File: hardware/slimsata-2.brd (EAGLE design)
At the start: 20.3 x 64.8 mm, 2 parts

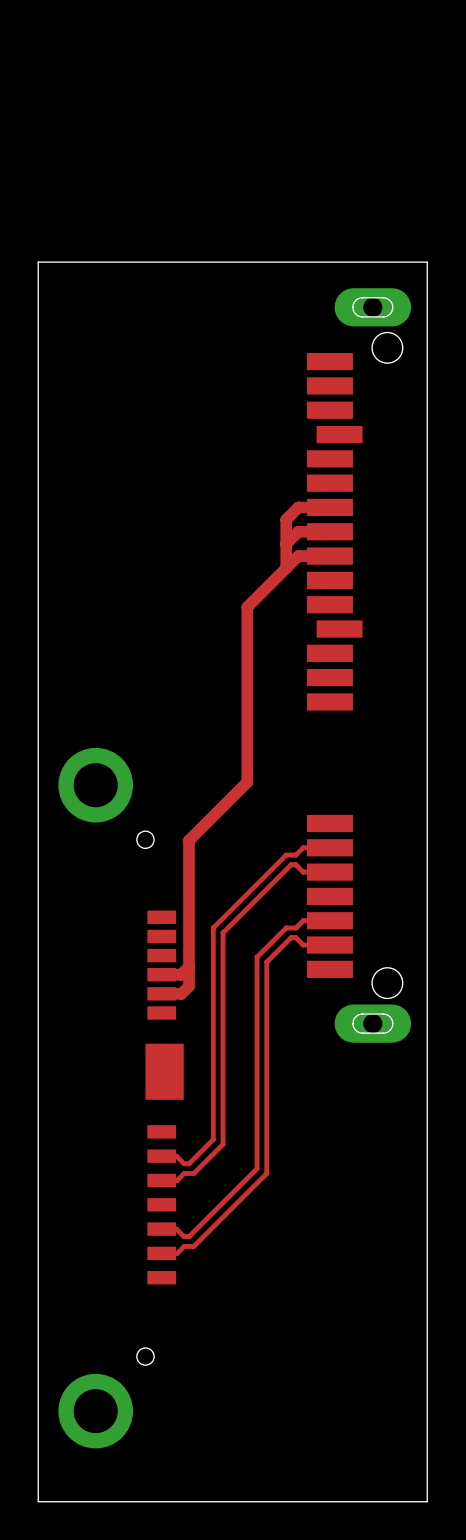
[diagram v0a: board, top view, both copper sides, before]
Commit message: Vias um Datenleitungen
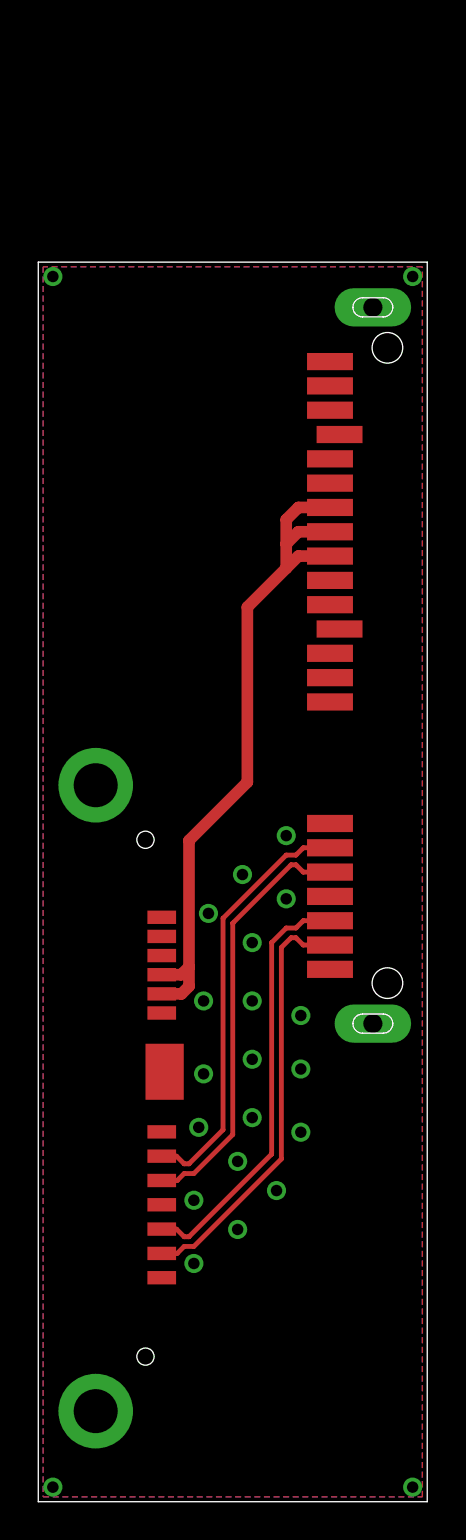
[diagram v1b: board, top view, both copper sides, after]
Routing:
- added copper zone on layer 1, net GND
- added copper zone on layer 16, net GND
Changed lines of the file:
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@@
 <wire x1="7.257" y1="12.972" x2="7.62" y2="13.335" width="0.254" layer="1"/>
 <wire x1="7.62" y1="13.335" x2="8.128" y2="13.335" width="0.254" layer="1"/>
-<wire x1="8.128" y1="13.335" x2="11.938" y2="17.145" width="0.254" layer="1"/>
-<wire x1="11.938" y1="17.145" x2="11.938" y2="28.194" width="0.254" layer="1"/>
-<wire x1="11.938" y1="28.194" x2="13.208" y2="29.464" width="0.254" layer="1"/>
+<wire x1="8.128" y1="13.335" x2="12.7" y2="17.907" width="0.254" layer="1"/>
+<wire x1="12.7" y1="17.907" x2="12.7" y2="28.956" width="0.254" layer="1"/>
+<wire x1="12.7" y1="28.956" x2="13.208" y2="29.464" width="0.254" layer="1"/>
 <wire x1="15.24" y1="29.083" x2="13.843" y2="29.083" width="0.254" layer="1"/>
 <wire x1="13.843" y1="29.083" x2="13.462" y2="29.464" width="0.254" layer="1"/>
@@
 <wire x1="7.221" y1="14.242" x2="7.62" y2="13.843" width="0.254" layer="1"/>
 <wire x1="7.62" y1="13.843" x2="7.874" y2="13.843" width="0.254" layer="1"/>
-<wire x1="7.874" y1="13.843" x2="11.43" y2="17.399" width="0.254" layer="1"/>
-<wire x1="11.43" y1="17.399" x2="11.43" y2="28.448" width="0.254" layer="1"/>
-<wire x1="11.43" y1="28.448" x2="12.954" y2="29.972" width="0.254" layer="1"/>
+<wire x1="7.874" y1="13.843" x2="12.192" y2="18.161" width="0.254" layer="1"/>
+<wire x1="12.192" y1="18.161" x2="12.192" y2="29.21" width="0.254" layer="1"/>
+<wire x1="12.192" y1="29.21" x2="12.954" y2="29.972" width="0.254" layer="1"/>
 <wire x1="15.24" y1="30.353" x2="13.843" y2="30.353" width="0.254" layer="1"/>
 <wire x1="13.843" y1="30.353" x2="13.462" y2="29.972" width="0.254" layer="1"/>
@@
 <wire x1="7.257" y1="16.782" x2="7.62" y2="17.145" width="0.254" layer="1"/>
 <wire x1="7.62" y1="17.145" x2="8.128" y2="17.145" width="0.254" layer="1"/>
-<wire x1="8.128" y1="17.145" x2="9.652" y2="18.669" width="0.254" layer="1"/>
-<wire x1="9.652" y1="29.718" x2="9.652" y2="18.669" width="0.254" layer="1"/>
-<wire x1="9.652" y1="29.718" x2="13.208" y2="33.274" width="0.254" layer="1"/>
+<wire x1="8.128" y1="17.145" x2="10.16" y2="19.177" width="0.254" layer="1"/>
+<wire x1="10.16" y1="30.226" x2="10.16" y2="19.177" width="0.254" layer="1"/>
+<wire x1="10.16" y1="30.226" x2="13.208" y2="33.274" width="0.254" layer="1"/>
 <wire x1="13.462" y1="33.274" x2="13.208" y2="33.274" width="0.254" layer="1"/>
 <wire x1="15.24" y1="32.893" x2="13.843" y2="32.893" width="0.254" layer="1"/>
@@
 <wire x1="7.221" y1="18.052" x2="7.62" y2="17.653" width="0.254" layer="1"/>
 <wire x1="7.62" y1="17.653" x2="7.874" y2="17.653" width="0.254" layer="1"/>
-<wire x1="7.874" y1="17.653" x2="9.144" y2="18.923" width="0.254" layer="1"/>
-<wire x1="9.144" y1="29.972" x2="9.144" y2="18.923" width="0.254" layer="1"/>
-<wire x1="9.144" y1="29.972" x2="12.954" y2="33.782" width="0.254" layer="1"/>
+<wire x1="7.874" y1="17.653" x2="9.652" y2="19.431" width="0.254" layer="1"/>
+<wire x1="9.652" y1="30.48" x2="9.652" y2="19.431" width="0.254" layer="1"/>
+<wire x1="9.652" y1="30.48" x2="12.954" y2="33.782" width="0.254" layer="1"/>
 <wire x1="15.24" y1="34.163" x2="13.843" y2="34.163" width="0.254" layer="1"/>
 <wire x1="13.843" y1="34.163" x2="13.462" y2="33.782" width="0.254" layer="1"/>
@@
 <contactref element="CON2" pad="P6"/>
 <contactref element="CON2" pad="P5"/>
-<wire x1="15.74" y1="55.753" x2="17.48" y2="62.398" width="0" layer="19" extent="1-1"/>
-<wire x1="15.24" y1="53.213" x2="15.74" y2="55.753" width="0" layer="19" extent="1-1"/>
-<wire x1="15.24" y1="48.133" x2="15.24" y2="53.213" width="0" layer="19" extent="1-1"/>
-<wire x1="15.24" y1="46.863" x2="15.24" y2="48.133" width="0" layer="19" extent="1-1"/>
-<wire x1="15.74" y1="45.593" x2="15.24" y2="46.863" width="0" layer="19" extent="1-1"/>
-<wire x1="15.24" y1="35.433" x2="15.74" y2="45.593" width="0" layer="19" extent="1-1"/>
-<wire x1="15.24" y1="31.623" x2="15.24" y2="35.433" width="0" layer="19" extent="1-1"/>
-<wire x1="15.24" y1="27.813" x2="15.24" y2="31.623" width="0" layer="19" extent="1-1"/>
-<wire x1="17.48" y1="24.978" x2="15.24" y2="27.813" width="0" layer="19" extent="1-1"/>
-<wire x1="3" y1="37.432" x2="15.24" y2="27.813" width="0" layer="19" extent="1-1"/>
-<wire x1="6.45" y1="30.532" x2="3" y2="37.432" width="0" layer="19" extent="1-1"/>
-<wire x1="6.45" y1="29.532" x2="6.45" y2="30.532" width="0" layer="19" extent="1-1"/>
-<wire x1="6.6" y1="22.462" x2="6.45" y2="29.532" width="0" layer="19" extent="1-1"/>
-<wire x1="6.45" y1="19.322" x2="6.6" y2="22.462" width="0" layer="19" extent="1-1"/>
-<wire x1="6.45" y1="15.512" x2="6.45" y2="19.322" width="0" layer="19" extent="1-1"/>
-<wire x1="6.45" y1="11.702" x2="6.45" y2="15.512" width="0" layer="19" extent="1-1"/>
-<wire x1="3" y1="4.732" x2="6.45" y2="11.702" width="0" layer="19" extent="1-1"/>
+<polygon width="0.6096" layer="1">
+<vertex x="0.254" y="0.254"/>
+<vertex x="20.066" y="0.254"/>
+<vertex x="20.066" y="64.516"/>
+<vertex x="0.254" y="64.516"/>
+</polygon>
+<polygon width="0.6096" layer="16">
+<vertex x="0.254" y="0.254"/>
+<vertex x="20.066" y="0.254"/>
+<vertex x="20.066" y="64.516"/>
+<vertex x="0.254" y="64.516"/>
+</polygon>
+<via x="0.762" y="0.762" extent="1-16" drill="0.6"/>
+<via x="19.558" y="0.762" extent="1-16" drill="0.6"/>
+<via x="0.762" y="64.008" extent="1-16" drill="0.6"/>
+<via x="19.558" y="64.008" extent="1-16" drill="0.6"/>
+<via x="8.128" y="15.748" extent="1-16" drill="0.6"/>
+<via x="10.414" y="17.78" extent="1-16" drill="0.6"/>
+<via x="11.176" y="20.066" extent="1-16" drill="0.6"/>
+<via x="11.176" y="23.114" extent="1-16" drill="0.6"/>
+<via x="11.176" y="26.162" extent="1-16" drill="0.6"/>
+<via x="11.176" y="29.21" extent="1-16" drill="0.6"/>
+<via x="12.954" y="31.496" extent="1-16" drill="0.6"/>
+<via x="8.382" y="19.558" extent="1-16" drill="0.6"/>
+<via x="8.636" y="22.352" extent="1-16" drill="0.6"/>
+<via x="8.636" y="26.162" extent="1-16" drill="0.6"/>
+<via x="8.89" y="30.734" extent="1-16" drill="0.6"/>
+<via x="10.668" y="32.766" extent="1-16" drill="0.6"/>
+<via x="12.954" y="34.798" extent="1-16" drill="0.6"/>
+<via x="8.128" y="12.446" extent="1-16" drill="0.6"/>
+<via x="10.414" y="14.224" extent="1-16" drill="0.6"/>
+<via x="12.446" y="16.256" extent="1-16" drill="0.6"/>
+<via x="13.716" y="19.304" extent="1-16" drill="0.6"/>
+<via x="13.716" y="22.606" extent="1-16" drill="0.6"/>
+<via x="13.716" y="25.4" extent="1-16" drill="0.6"/>
 </signal>
 </signals>

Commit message: Masse von Hand verlegt
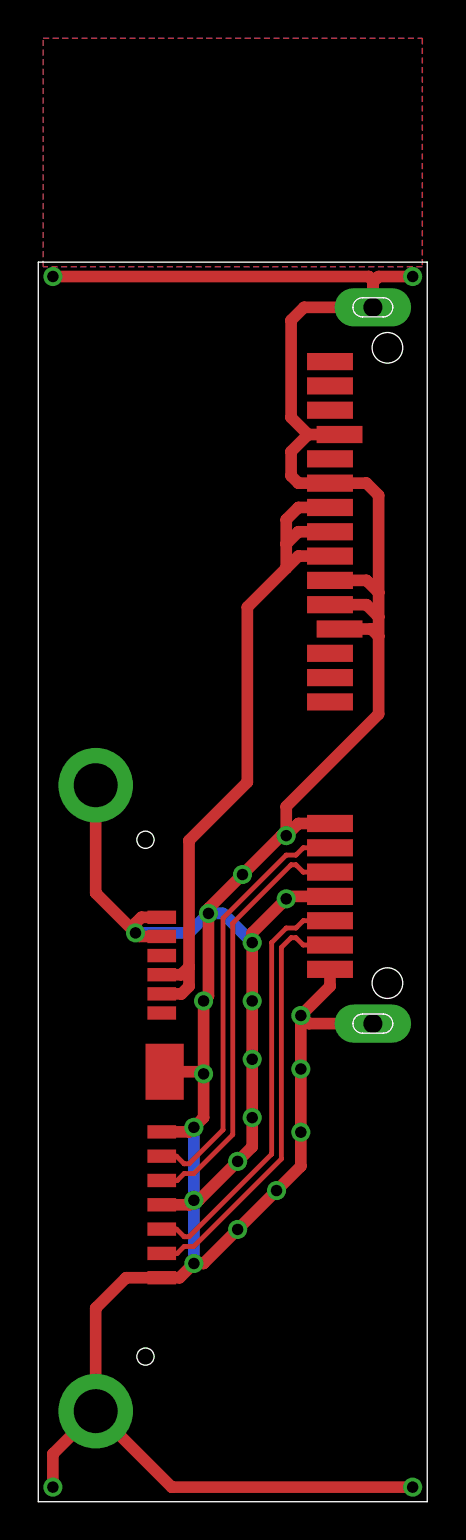
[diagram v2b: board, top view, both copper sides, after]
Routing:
- net GND: track 0.00 -> 198.4 mm, vias 23 -> 24
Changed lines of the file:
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@@
 <contactref element="CON2" pad="P5"/>
 <polygon width="0.6096" layer="1">
-<vertex x="0.254" y="0.254"/>
-<vertex x="20.066" y="0.254"/>
+<vertex x="0.254" y="76.454"/>
+<vertex x="20.066" y="76.454"/>
 <vertex x="20.066" y="64.516"/>
 <vertex x="0.254" y="64.516"/>
 </polygon>
 <polygon width="0.6096" layer="16">
-<vertex x="0.254" y="0.254"/>
-<vertex x="20.066" y="0.254"/>
+<vertex x="0.254" y="76.454"/>
+<vertex x="20.066" y="76.454"/>
 <vertex x="20.066" y="64.516"/>
 <vertex x="0.254" y="64.516"/>
@@
 <via x="11.176" y="29.21" extent="1-16" drill="0.6"/>
 <via x="12.954" y="31.496" extent="1-16" drill="0.6"/>
-<via x="8.382" y="19.558" extent="1-16" drill="0.6"/>
+<via x="8.128" y="19.558" extent="1-16" drill="0.6"/>
 <via x="8.636" y="22.352" extent="1-16" drill="0.6"/>
 <via x="8.636" y="26.162" extent="1-16" drill="0.6"/>
@@
 <via x="13.716" y="22.606" extent="1-16" drill="0.6"/>
 <via x="13.716" y="25.4" extent="1-16" drill="0.6"/>
+<wire x1="6.45" y1="11.702" x2="7.384" y2="11.702" width="0.6096" layer="1"/>
+<wire x1="8.128" y1="12.446" x2="8.636" y2="12.446" width="0.6096" layer="1"/>
+<wire x1="8.636" y1="12.446" x2="10.414" y2="14.224" width="0.6096" layer="1"/>
+<wire x1="10.414" y1="14.224" x2="12.446" y2="16.256" width="0.6096" layer="1"/>
+<wire x1="12.446" y1="16.256" x2="13.716" y2="17.526" width="0.6096" layer="1"/>
+<wire x1="13.716" y1="17.526" x2="13.716" y2="19.304" width="0.6096" layer="1"/>
+<wire x1="13.716" y1="22.606" x2="13.716" y2="19.304" width="0.6096" layer="1"/>
+<wire x1="13.716" y1="25.4" x2="13.716" y2="22.606" width="0.6096" layer="1"/>
+<wire x1="6.45" y1="15.512" x2="7.892" y2="15.512" width="0.6096" layer="1"/>
+<wire x1="7.892" y1="15.512" x2="8.128" y2="15.748" width="0.6096" layer="1"/>
+<wire x1="8.128" y1="15.748" x2="8.382" y2="15.748" width="0.6096" layer="1"/>
+<wire x1="8.382" y1="15.748" x2="10.414" y2="17.78" width="0.6096" layer="1"/>
+<wire x1="10.414" y1="17.78" x2="11.176" y2="18.542" width="0.6096" layer="1"/>
+<wire x1="11.176" y1="18.542" x2="11.176" y2="20.066" width="0.6096" layer="1"/>
+<wire x1="11.176" y1="23.114" x2="11.176" y2="20.066" width="0.6096" layer="1"/>
+<wire x1="11.176" y1="23.114" x2="11.176" y2="26.162" width="0.6096" layer="1"/>
+<wire x1="11.176" y1="26.162" x2="11.176" y2="29.21" width="0.6096" layer="1"/>
+<wire x1="11.176" y1="29.21" x2="11.176" y2="29.718" width="0.6096" layer="1"/>
+<wire x1="11.176" y1="29.718" x2="12.954" y2="31.496" width="0.6096" layer="1"/>
+<wire x1="15.24" y1="31.623" x2="13.081" y2="31.623" width="0.6096" layer="1"/>
+<wire x1="13.081" y1="31.623" x2="12.954" y2="31.496" width="0.6096" layer="1"/>
+<wire x1="15.24" y1="27.813" x2="15.24" y2="26.924" width="0.6096" layer="1"/>
+<wire x1="15.24" y1="26.924" x2="13.716" y2="25.4" width="0.6096" layer="1"/>
+<wire x1="17.48" y1="24.978" x2="14.138" y2="24.978" width="0.6096" layer="1"/>
+<wire x1="14.138" y1="24.978" x2="13.716" y2="25.4" width="0.6096" layer="1"/>
+<wire x1="15.24" y1="35.433" x2="13.589" y2="35.433" width="0.6096" layer="1"/>
+<wire x1="13.589" y1="35.433" x2="12.954" y2="34.798" width="0.6096" layer="1"/>
+<wire x1="12.954" y1="34.798" x2="12.7" y2="34.798" width="0.6096" layer="1"/>
+<wire x1="12.7" y1="34.798" x2="10.668" y2="32.766" width="0.6096" layer="1"/>
+<wire x1="8.89" y1="30.734" x2="8.89" y2="30.988" width="0.6096" layer="1"/>
+<wire x1="8.89" y1="30.988" x2="10.668" y2="32.766" width="0.6096" layer="1"/>
+<wire x1="8.89" y1="26.416" x2="8.636" y2="26.162" width="0.6096" layer="1"/>
+<wire x1="8.636" y1="22.352" x2="8.636" y2="26.162" width="0.6096" layer="1"/>
+<wire x1="6.45" y1="29.532" x2="5.266" y2="29.532" width="0.6096" layer="1"/>
+<wire x1="5.266" y1="29.532" x2="5.08" y2="29.718" width="0.6096" layer="1"/>
+<wire x1="6.45" y1="30.532" x2="5.386" y2="30.532" width="0.6096" layer="1"/>
+<wire x1="5.386" y1="30.532" x2="5.08" y2="30.226" width="0.6096" layer="1"/>
+<via x="5.08" y="29.718" extent="1-16" drill="0.6"/>
+<wire x1="5.08" y1="29.718" x2="7.874" y2="29.718" width="0.6096" layer="16"/>
+<wire x1="7.874" y1="29.718" x2="8.89" y2="30.734" width="0.6096" layer="16"/>
+<wire x1="5.08" y1="30.226" x2="5.08" y2="29.718" width="0.6096" layer="1"/>
+<wire x1="3" y1="37.432" x2="3" y2="31.798" width="0.6096" layer="1"/>
+<wire x1="3" y1="31.798" x2="5.08" y2="29.718" width="0.6096" layer="1"/>
+<wire x1="3" y1="4.732" x2="3" y2="10.112" width="0.6096" layer="1"/>
+<wire x1="3" y1="10.112" x2="4.59" y2="11.702" width="0.6096" layer="1"/>
+<wire x1="6.45" y1="11.702" x2="4.59" y2="11.702" width="0.6096" layer="1"/>
+<wire x1="0.762" y1="0.762" x2="0.762" y2="2.494" width="0.6096" layer="1"/>
+<wire x1="0.762" y1="2.494" x2="3" y2="4.732" width="0.6096" layer="1"/>
+<wire x1="19.558" y1="0.762" x2="6.97" y2="0.762" width="0.6096" layer="1"/>
+<wire x1="6.97" y1="0.762" x2="3" y2="4.732" width="0.6096" layer="1"/>
+<wire x1="17.48" y1="62.398" x2="17.48" y2="63.708" width="0.6096" layer="1"/>
+<wire x1="17.48" y1="63.708" x2="17.78" y2="64.008" width="0.6096" layer="1"/>
+<wire x1="17.78" y1="64.008" x2="19.558" y2="64.008" width="0.6096" layer="1"/>
+<wire x1="17.48" y1="62.398" x2="17.48" y2="63.8" width="0.6096" layer="1"/>
+<wire x1="17.48" y1="63.8" x2="17.272" y2="64.008" width="0.6096" layer="1"/>
+<wire x1="17.272" y1="64.008" x2="0.762" y2="64.008" width="0.6096" layer="1"/>
+<wire x1="17.48" y1="62.398" x2="13.884" y2="62.398" width="0.6096" layer="1"/>
+<wire x1="13.884" y1="62.398" x2="13.208" y2="61.722" width="0.6096" layer="1"/>
+<wire x1="13.208" y1="61.722" x2="13.208" y2="56.642" width="0.6096" layer="1"/>
+<wire x1="14.097" y1="55.753" x2="13.208" y2="56.642" width="0.6096" layer="1"/>
+<wire x1="15.74" y1="55.753" x2="14.097" y2="55.753" width="0.6096" layer="1"/>
+<wire x1="14.097" y1="55.753" x2="13.208" y2="54.864" width="0.6096" layer="1"/>
+<wire x1="13.208" y1="54.864" x2="13.208" y2="53.594" width="0.6096" layer="1"/>
+<wire x1="15.24" y1="53.213" x2="13.589" y2="53.213" width="0.6096" layer="1"/>
+<wire x1="13.589" y1="53.213" x2="13.208" y2="53.594" width="0.6096" layer="1"/>
+<wire x1="15.24" y1="53.213" x2="17.145" y2="53.213" width="0.6096" layer="1"/>
+<wire x1="17.145" y1="53.213" x2="17.78" y2="52.578" width="0.6096" layer="1"/>
+<wire x1="17.78" y1="52.578" x2="17.78" y2="47.498" width="0.6096" layer="1"/>
+<wire x1="17.78" y1="47.498" x2="17.78" y2="46.228" width="0.6096" layer="1"/>
+<wire x1="17.78" y1="46.228" x2="17.78" y2="45.212" width="0.6096" layer="1"/>
+<wire x1="17.78" y1="45.212" x2="17.78" y2="41.148" width="0.6096" layer="1"/>
+<wire x1="15.24" y1="48.133" x2="17.145" y2="48.133" width="0.6096" layer="1"/>
+<wire x1="17.145" y1="48.133" x2="17.78" y2="47.498" width="0.6096" layer="1"/>
+<wire x1="15.24" y1="46.863" x2="17.145" y2="46.863" width="0.6096" layer="1"/>
+<wire x1="17.145" y1="46.863" x2="17.78" y2="46.228" width="0.6096" layer="1"/>
+<wire x1="15.74" y1="45.593" x2="17.399" y2="45.593" width="0.6096" layer="1"/>
+<wire x1="17.399" y1="45.593" x2="17.78" y2="45.212" width="0.6096" layer="1"/>
+<wire x1="17.78" y1="41.148" x2="12.954" y2="36.322" width="0.6096" layer="1"/>
+<wire x1="12.954" y1="36.322" x2="12.954" y2="34.798" width="0.6096" layer="1"/>
+<wire x1="6.45" y1="19.322" x2="7.892" y2="19.322" width="0.6096" layer="1"/>
+<wire x1="7.892" y1="19.322" x2="8.128" y2="19.558" width="0.6096" layer="1"/>
+<wire x1="8.89" y1="30.734" x2="9.652" y2="30.734" width="0.6096" layer="16"/>
+<wire x1="9.652" y1="30.734" x2="11.176" y2="29.21" width="0.6096" layer="16"/>
+<wire x1="8.89" y1="26.416" x2="8.89" y2="30.734" width="0.6096" layer="1"/>
+<wire x1="8.128" y1="19.558" x2="8.128" y2="15.748" width="0.6096" layer="16"/>
+<wire x1="8.128" y1="12.446" x2="8.128" y2="15.748" width="0.6096" layer="16"/>
+<wire x1="7.384" y1="11.702" x2="8.128" y2="12.446" width="0.6096" layer="1"/>
+<wire x1="8.636" y1="22.352" x2="8.636" y2="20.066" width="0.6096" layer="1"/>
+<wire x1="8.636" y1="20.066" x2="8.128" y2="19.558" width="0.6096" layer="1"/>
+<wire x1="8.526" y1="22.462" x2="6.6" y2="22.462" width="0.6096" layer="1"/>
+<wire x1="8.636" y1="22.352" x2="8.526" y2="22.462" width="0" layer="19" extent="1-1"/>
 </signal>
 </signals>
